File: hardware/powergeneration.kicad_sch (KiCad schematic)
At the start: 18 parts, among them U5 AOZ1284PI, U6 TL431BIDBZR

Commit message: powergeneration: C16 footprint 0402 -> 1210 (REV_C 3.3 #15)
47 uF 0402 footprint'iyle atanmıştı; bu değer 0402'de üretilmiyor.
C_1210_3225Metric'e çevrildi (C12/C13 ile aynı).

Co-Authored-By: Claude Opus 5 <noreply@anthropic.com>
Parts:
- C16: footprint Capacitor_SMD:C_0402_1005Metric -> Capacitor_SMD:C_1210_3225Metric
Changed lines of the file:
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@@
 			)
 		)
-		(property "Footprint" "Capacitor_SMD:C_0402_1005Metric"
+		(property "Footprint" "Capacitor_SMD:C_1210_3225Metric"
 			(at 218.44 88.9 0)
 			(hide yes)

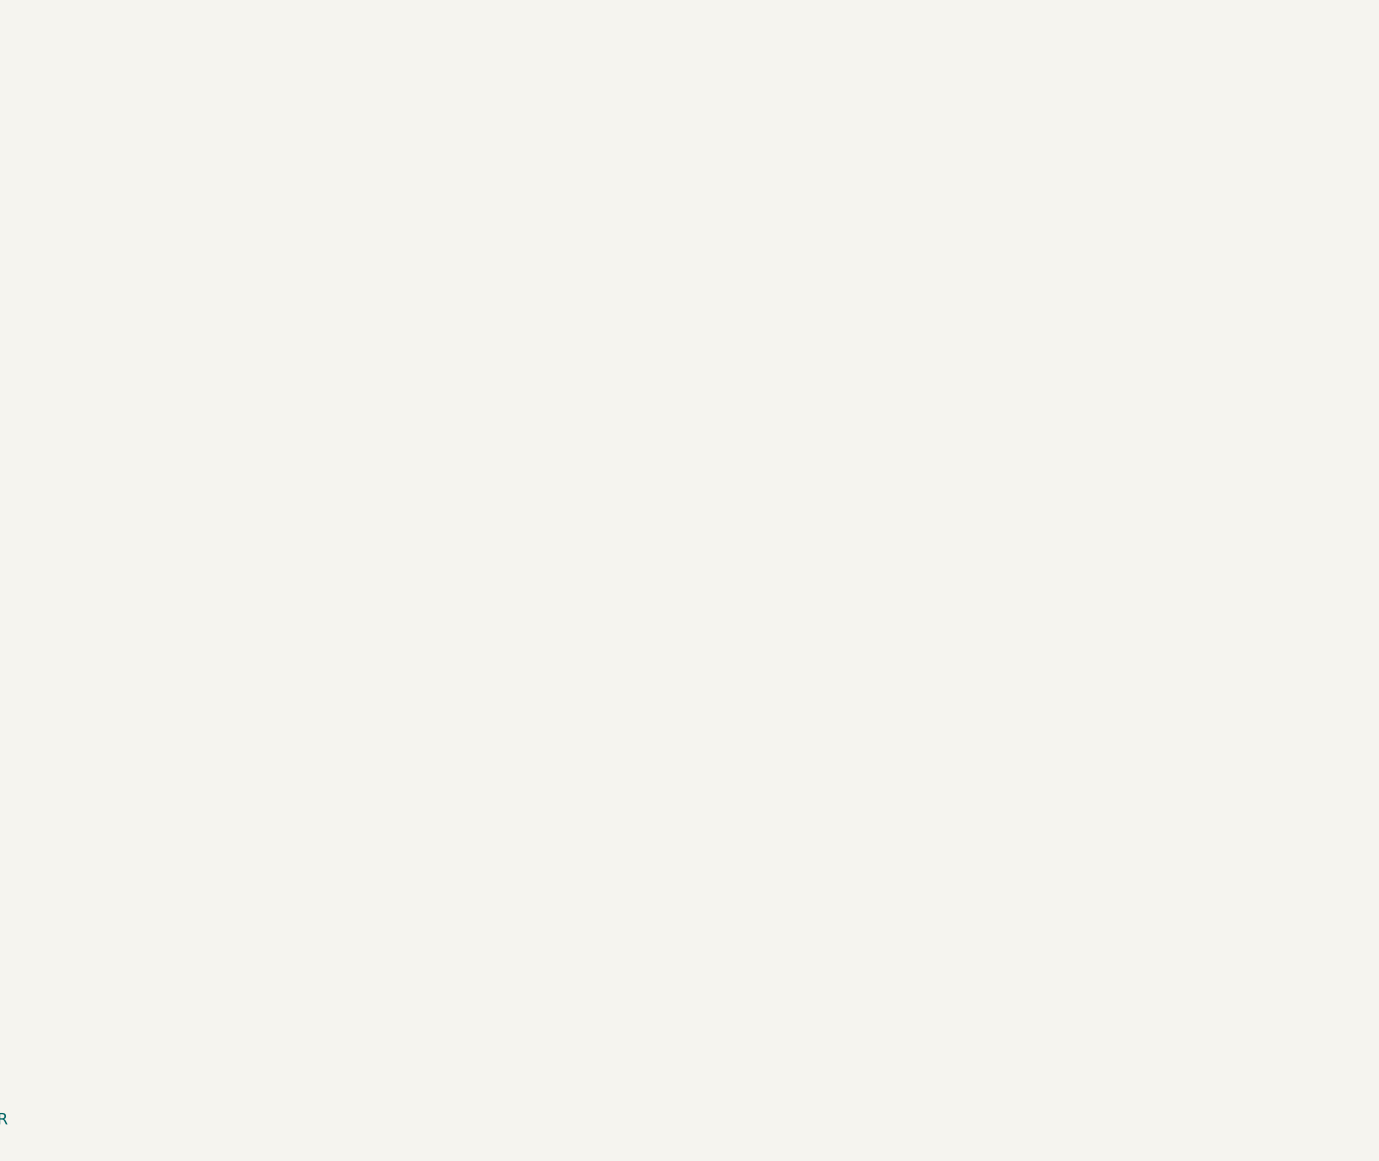
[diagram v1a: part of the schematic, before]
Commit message: powergeneration: TPS55340 pre-boost bloğunu ekle (REV_C 3.3 #1-#12)
PD_VOUT 5 V'un altına indiğinde (3.3 V PPS) dahili rail'i ayakta tutan,
üstünde pass-through çalışan asenkron boost. Yeni net: V_PRE (global).

Bileşenler (18): U11 TPS55340PWPR, L3 6.8uH TBD, D4 Schottky TBD,
D5 BAT54 (FB clamp), R47 78.7k FREQ, R48/R49 30.1k/9.76k FB bölücü,
R50/R51 820R/1k clamp bias, R52 2k + C24 100nF kompanzasyon, R53 100k EN,
C23 47nF SS, C25/C26 giriş, C27/C28 çıkış, C29 47uF sönümleme bulk.

Doküman 3.3 #8 "R3 = 2k, C4 = 100nF" TI uygulama notunun eleman adlarıydı;
kartta R3 ve C4 zaten başka parçalar. Yeni referans atandı: R52 ve C24.

Doğrulama
- 10 yeni netin tamamı netlist'te beklendiği gibi; U11'in AGND/PGND/
  PowerPAD/SYNC/NC pinlerinin hepsi GND'de.
- ERC 4'te sabit kaldı, tek yeni ihlal yok.
- FB clamp kontrolü: 28 V pass-through'da FB ~2.43 V (abs max 3 V).

Notlar
- Sayfa A4 -> A3; blok A4'e sığmıyordu.
- TPS55340 sembolünde PGND 13/14 pinlerinin gizliliği kaldırıldı. KiCad
  gizli power_in pinlerini ada göre otomatik bağlıyor, bu yüzden PGND
  netine kaçıyorlardı.
- Yerleşim üretilmiş haliyle dağınık; elektriksel olarak doğru, KiCad'de
  düzenlenmeyi bekliyor.

Co-Authored-By: Claude Opus 5 <noreply@anthropic.com>
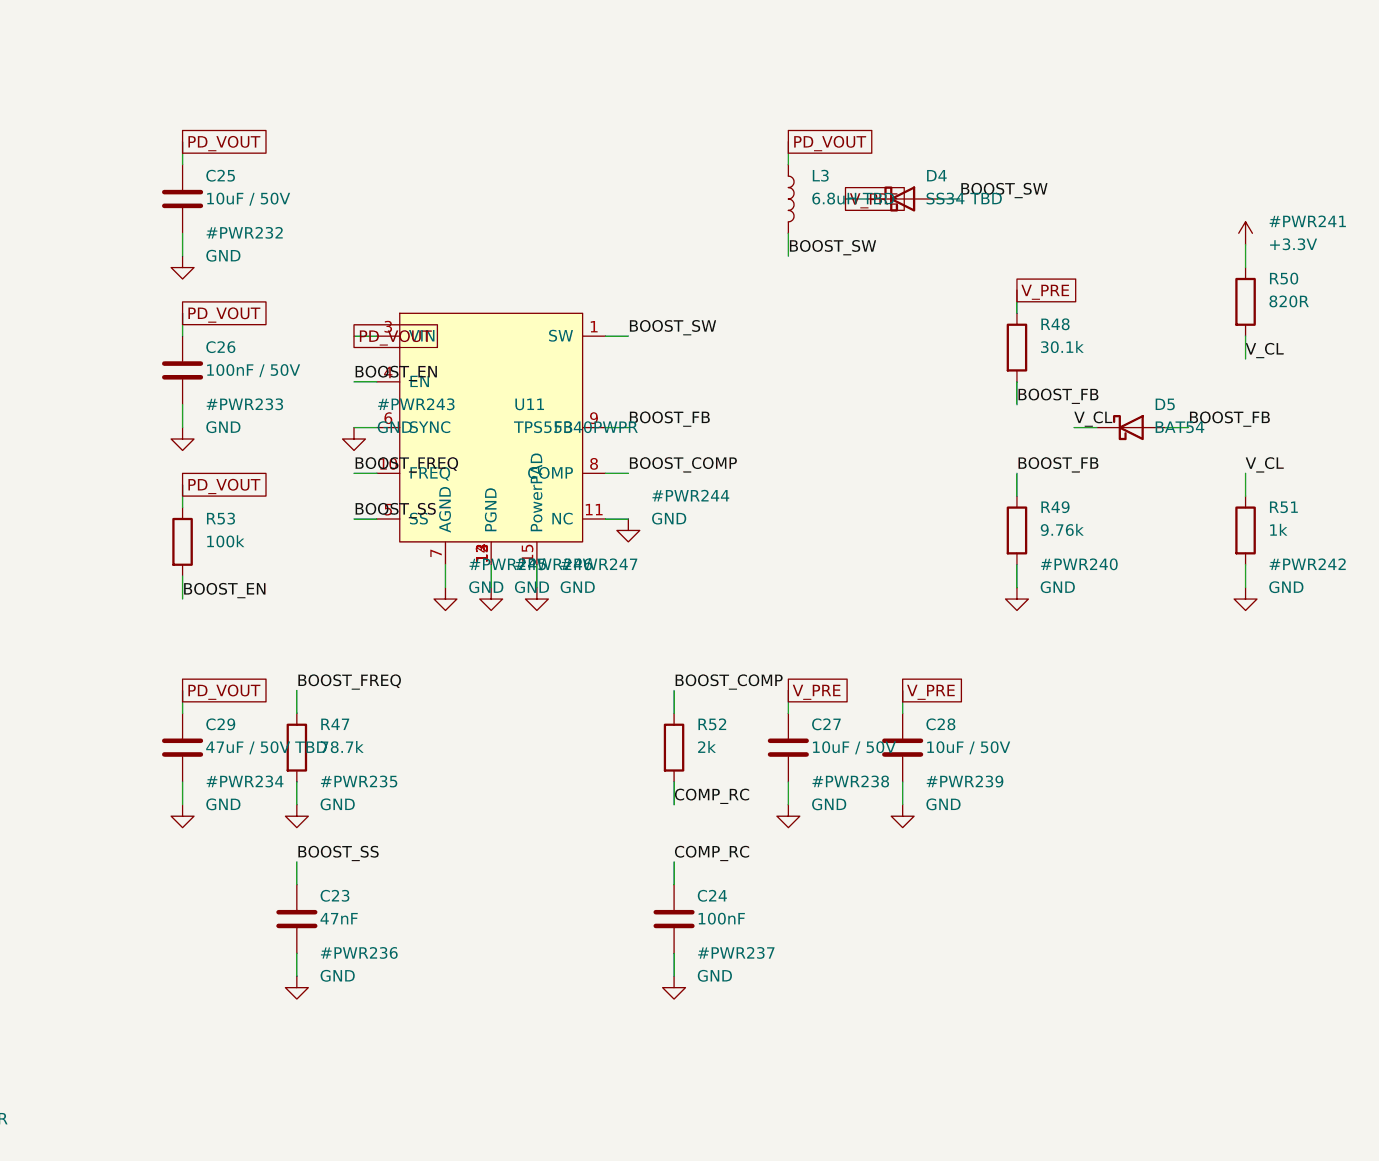
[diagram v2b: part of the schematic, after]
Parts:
- added C23: 47nF, Capacitor_SMD:C_0402_1005Metric, symbol Device:C
- added C24: 100nF, Capacitor_SMD:C_0402_1005Metric, symbol Device:C
- added C25, C27, C28: 10uF / 50V, Capacitor_SMD:C_1210_3225Metric, symbol Device:C
- added C26: 100nF / 50V, Capacitor_SMD:C_0402_1005Metric, symbol Device:C
- added C29: 47uF / 50V TBD, Capacitor_SMD:C_1210_3225Metric, symbol Device:C
- added D4: SS34 TBD, Diode_SMD:D_SMA, symbol Device:D_Schottky
- added D5: BAT54, Diode_SMD:D_SOD-123, symbol Device:D_Schottky
- added L3: 6.8uH TBD, Inductor_SMD:L_1210_3225Metric, symbol Device:L
- added R47: 78.7k, Resistor_SMD:R_0402_1005Metric, symbol Device:R
- added R48: 30.1k, Resistor_SMD:R_0402_1005Metric, symbol Device:R
- added R49: 9.76k, Resistor_SMD:R_0402_1005Metric, symbol Device:R
- added R50: 820R, Resistor_SMD:R_0402_1005Metric, symbol Device:R
- added R51: 1k, Resistor_SMD:R_0402_1005Metric, symbol Device:R
- added R52: 2k, Resistor_SMD:R_0402_1005Metric, symbol Device:R
- added R53: 100k, Resistor_SMD:R_0402_1005Metric, symbol Device:R
- added U11: TPS55340PWPR, Package_SO:Texas_HTSSOP-14-1EP_4.4x5mm_P0.65mm_EP3.4x5mm_Mask3.155x3.255mm_ThermalVias, symbol Power_Path_Custom:TPS55340PWPR
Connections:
- net +3.3V: now also R50.1
- net GND: now also C23.2, C24.2, C25.2, C26.2, C27.2, C28.2, C29.2, R47.2, R49.2, R51.2, U11.11 (NC), U11.12 (PGND), U11.13 (PGND), U11.14 (PGND), U11.15 (PowerPAD), U11.6 (SYNC), U11.7 (AGND)
- net PD_VOUT: now also C25.1, C26.1, C29.1, L3.1, R53.1, U11.3 (VIN)
- new net BOOST_COMP: R52.1, U11.8 (COMP)
- new net BOOST_EN: R53.2, U11.4 (EN)
- new net BOOST_FB: D5.2 (A), R48.2, R49.1, U11.9 (FB)
- new net BOOST_FREQ: R47.1, U11.10 (FREQ)
- new net BOOST_SS: C23.1, U11.5 (SS)
- new net BOOST_SW: D4.2 (A), L3.2, U11.1 (SW), U11.2 (SW)
- new net COMP_RC: C24.1, R52.2
- new net V_CL: D5.1 (K), R50.2, R51.1
- new net V_PRE: C27.1, C28.1, D4.1 (K), R48.1

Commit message: powergeneration: dahili rail'i V_PRE'ye taşı (REV_C 3.3 #13, #14)
AOZ1284 buck ve TL431 EN bias'ı artık PD_VOUT yerine pre-boost çıkışı
V_PRE'den besleniyor. Böylece PD_VOUT 3.3 V PPS'e indiğinde dahili rail
5.02 V'ta kalıyor.

Sayfadaki iki PD_VOUT global etiketi V_PRE olarak değiştirildi:
- (29.21, 71.12)   -> AOZ1284 VIN + giriş kapasite bankası
- (243.84, 110.49) -> R43 / TL431 EN bias

Doküman 3.3 #13 yalnızca C12/C13'ü sayıyor; gerçekte aynı düğümde C14
(100nF HF bypass) da var, aynı sırada ve aynı nette. VIN ile birlikte
taşındı, aksi halde bypass yanlış düğümde kalırdı. C8, R13 ve TP3 başka
sayfalarda ve PD_VOUT'ta kaldı (R13, AP33772S'in VOUT sense'i).

V_PRE için PWR_FLAG eklendi; boost çıkışı D4'ün passive katodundan
geldiği için ray "driven" görünmüyordu (power_pin_not_driven hatası).

Doğrulama
- V_PRE: C12.1, C13.1, C14.1, C27.1, C28.1, D4.1, R43.1, R48.1, U5.9
- PD_VOUT tam olarak bu 5 düğümü kaybetti, başka değişiklik yok
- PD_VOUT toplam kapasite 67.1 uF nominal, cSnkBulkPd 100 uF sınırı altında
- PD_VBUS_SENSED 2.2 uF, cSnkBulk 10 uF sınırı altında
- ERC 4'te sabit

Co-Authored-By: Claude Opus 5 <noreply@anthropic.com>
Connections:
- net PD_VOUT: no longer C12.1, C13.1, C14.1, R43.1, U5.9 (VIN)
- net V_PRE: now also C12.1, C13.1, C14.1, R43.1, U5.9 (VIN)
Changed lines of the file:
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@@
 		)
 	)
-	(global_label "PD_VOUT"
+	(global_label "V_PRE"
 		(shape passive)
 		(at 243.84 110.49 0)
@@
 		)
 	)
-	(global_label "PD_VOUT"
+	(global_label "V_PRE"
 		(shape passive)
 		(at 29.21 71.12 180)
@@
 			)
 		)
+	)
+	(symbol
+		(lib_id "power:PWR_FLAG")
+		(at 332.74 92.71 0)
+		(unit 1)
+		(body_style 1)
+		(exclude_from_sim no)
+		(in_bom yes)
+		(on_board yes)
+		(in_pos_files yes)
+		(dnp no)
+		(fields_autoplaced yes)
+		(property "Reference" "#FLG248"
+			(at 335.28 90.17 0)
+			(show_name no)
+			(do_not_autoplace no)
+			(effects
+				(font
+					(size 1.27 1.27)
+				)
+				(justify left)
+			)
+		)
+		(property "Value" "PWR_FLAG"
+			(at 335.28 92.71 0)
+			(show_name no)
+			(do_not_autoplace no)
+			(effects
+				(font
+					(size 1.27 1.27)
+				)
+				(justify left)
+			)
+		)
+		(property "Datasheet" "~"
+			(at 332.74 92.71 0)
+			(hide yes)
+			(show_name no)
+			(do_not_autoplace no)
+			(effects
+				(font
+					(size 1.27 1.27)
+				)
+			)
+		)
+		(pin "1"
+		)
+		(instances
+			(project "gopo"
+				(path "/a43081a6-9aa2-4898-9347-bbcb5849dafd/5dec5942-8798-43d7-9ae8-350e99f1540a"
+					(reference "#FLG248")
+					(unit 1)
+				)
+			)
+		)
+	)
+	(wire
+		(pts
+			(xy 332.74 92.71) (xy 332.74 88.9)
+		)
+		(stroke
+			(width 0)
+			(type default)
+		)
+	)
+	(global_label "V_PRE"
+		(shape passive)
+		(at 332.74 88.9 0)
+		(fields_autoplaced yes)
+		(effects
+			(font
+				(size 1.27 1.27)
+			)
+			(justify left)
+		)
+		(property "Intersheetrefs" "${INTERSHEET_REFS}"
+			(at 332.74 88.9 0)
+			(hide yes)
+			(show_name no)
+			(do_not_autoplace no)
+			(effects
+				(font
+					(size 1.27 1.27)
+				)
+				(justify left)
+			)
+		)
